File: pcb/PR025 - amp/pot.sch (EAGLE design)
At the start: 25 parts, among them IC1 LM317, IC2 LM337, X1 22-23-2031, X2 22-23-2021

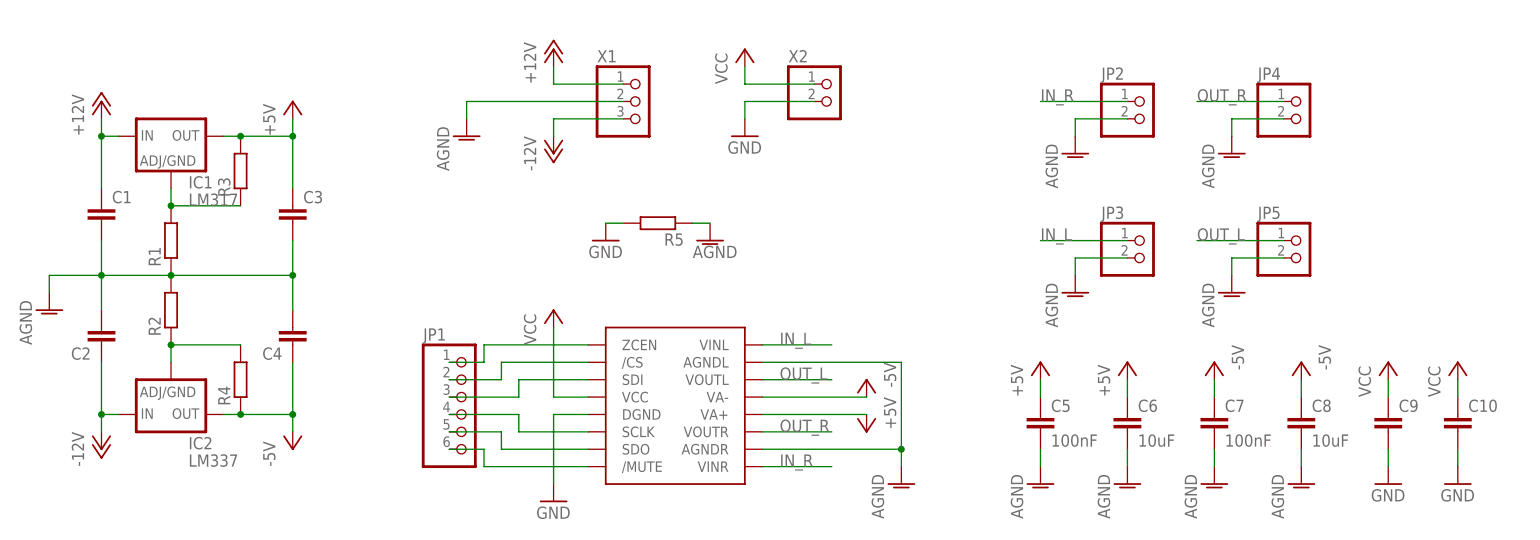
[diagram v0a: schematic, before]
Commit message: 
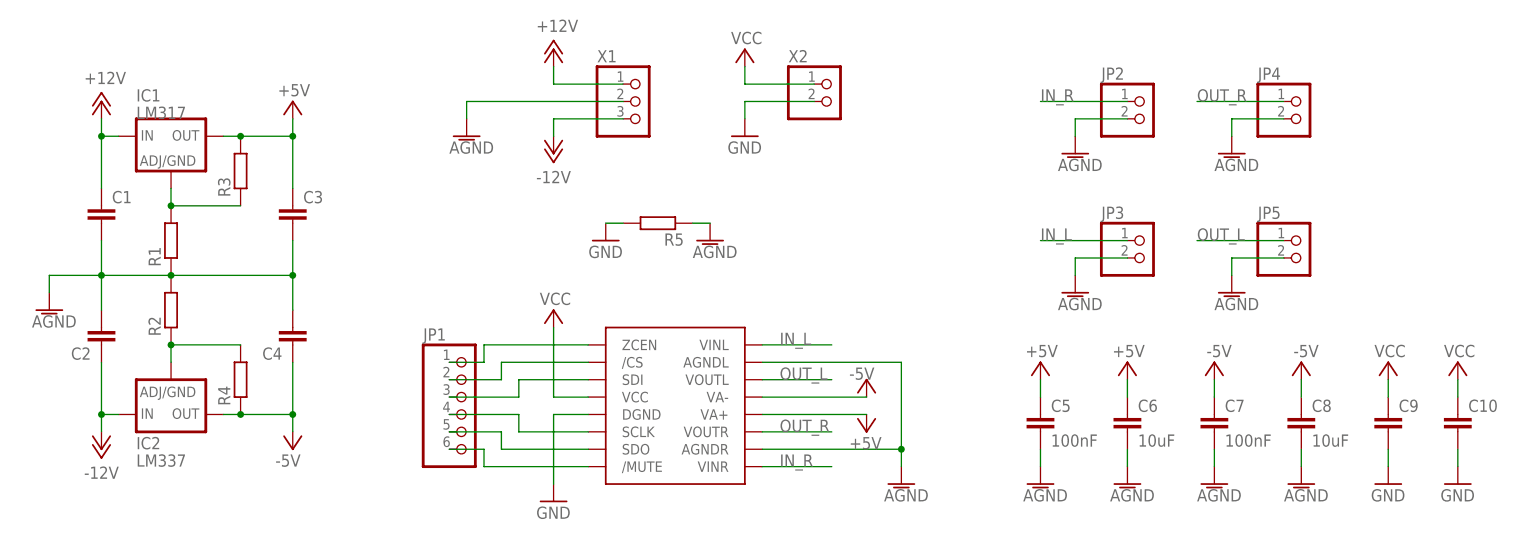
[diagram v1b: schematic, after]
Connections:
- net N$10 renamed SDO
- net N$11 renamed SCLK
- net N$6 renamed ZCEN
- net N$7 renamed /CS
- net N$8 renamed SDI
- net N$9 renamed /MUTE

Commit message: 
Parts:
- C1, C2: value (none) -> 1uF
- C10: value (none) -> 100nF
- C3, C4, C9: value (none) -> 10uF
- R1, R2: value (none) -> 680
- R3, R4: value (none) -> 220
- R5: value (none) -> 0
- U1: value (none) -> PGA2311
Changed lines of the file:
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@@
 <?xml version="1.0" encoding="utf-8"?>
 <!DOCTYPE eagle SYSTEM "eagle.dtd">
-<eagle version="6.5.0">
+<eagle version="6.6.0">
 <drawing>
 <settings>
@@
 <part name="AGND6" library="amp" deviceset="AGND" device="" value="AGND"/>
 <part name="AGND10" library="amp" deviceset="AGND" device="" value="AGND"/>
-<part name="U1" library="amp" deviceset="PGA2311" device=""/>
+<part name="U1" library="amp" deviceset="PGA2311" device="" value="PGA2311"/>
 <part name="AGND4" library="amp" deviceset="AGND" device="" value="AGND"/>
 <part name="C5" library="amp" deviceset="C-EU" device="C0805K" value="100nF"/>
@@
 <part name="IC1" library="amp" deviceset="LM317" device=""/>
 <part name="IC2" library="amp" deviceset="LM337" device=""/>
-<part name="R3" library="amp" deviceset="R-EU_" device=""/>
+<part name="R3" library="amp" deviceset="R-EU_" device="" value="220"/>
 <part name="P+7" library="amp" deviceset="+5V" device=""/>
 <part name="P+8" library="amp" deviceset="+5V" device=""/>
@@
 <part name="AGND12" library="amp" deviceset="AGND" device="" value="AGND"/>
 <part name="P+6" library="amp" deviceset="+5V" device=""/>
-<part name="R1" library="amp" deviceset="R-EU_" device=""/>
-<part name="R2" library="amp" deviceset="R-EU_" device=""/>
-<part name="R4" library="amp" deviceset="R-EU_" device=""/>
+<part name="R1" library="amp" deviceset="R-EU_" device="" value="680"/>
+<part name="R2" library="amp" deviceset="R-EU_" device="" value="680"/>
+<part name="R4" library="amp" deviceset="R-EU_" device="" value="220"/>
 <part name="P+1" library="amp" deviceset="+12V" device=""/>
 <part name="P-1" library="amp" deviceset="-12V" device=""/>
 <part name="P+2" library="amp" deviceset="+5V" device=""/>
-<part name="C1" library="amp" deviceset="C-EU" device="C0805K"/>
-<part name="C2" library="amp" deviceset="C-EU" device="C0805K"/>
-<part name="C4" library="amp" deviceset="C-EU" device="C0805K"/>
-<part name="C3" library="amp" deviceset="C-EU" device="C0805K"/>
+<part name="C1" library="amp" deviceset="C-EU" device="C0805K" value="1uF"/>
+<part name="C2" library="amp" deviceset="C-EU" device="C0805K" value="1uF"/>
+<part name="C4" library="amp" deviceset="C-EU" device="C0805K" value="10uF"/>
+<part name="C3" library="amp" deviceset="C-EU" device="C0805K" value="10uF"/>
 <part name="AGND1" library="amp" deviceset="AGND" device=""/>
 <part name="GND2" library="amp" deviceset="GND" device=""/>
-<part name="R5" library="amp" deviceset="R-EU_" device=""/>
+<part name="R5" library="amp" deviceset="R-EU_" device="" value="0"/>
 <part name="AGND3" library="amp" deviceset="AGND" device="" value="AGND"/>
 <part name="GND1" library="amp" deviceset="GND" device=""/>
 <part name="X2" library="amp" deviceset="22-23-2021" device="" value=""/>
 <part name="GND3" library="amp" deviceset="GND" device=""/>
-<part name="C9" library="amp" deviceset="C-EU" device="C0805K"/>
-<part name="C10" library="amp" deviceset="C-EU" device="C0805K"/>
+<part name="C9" library="amp" deviceset="C-EU" device="C0805K" value="10uF"/>
+<part name="C10" library="amp" deviceset="C-EU" device="C0805K" value="100nF"/>
 <part name="GND4" library="amp" deviceset="GND" device=""/>
 <part name="GND5" library="amp" deviceset="GND" device=""/>
@@
 </instance>
 <instance part="C2" gate="G$1" x="-12.7" y="134.62" smashed="yes" rot="R180">
-<attribute name="NAME" x="-14.224" y="134.239" size="1.778" layer="95" rot="R180"/>
-<attribute name="VALUE" x="-14.224" y="139.319" size="1.778" layer="96" rot="R180"/>
+<attribute name="NAME" x="-11.176" y="137.541" size="1.778" layer="95"/>
+<attribute name="VALUE" x="-11.176" y="132.461" size="1.778" layer="96"/>
 </instance>
 <instance part="C4" gate="G$1" x="15.24" y="134.62" smashed="yes" rot="R180">
-<attribute name="NAME" x="13.716" y="134.239" size="1.778" layer="95" rot="R180"/>
-<attribute name="VALUE" x="13.716" y="139.319" size="1.778" layer="96" rot="R180"/>
+<attribute name="NAME" x="16.764" y="137.541" size="1.778" layer="95"/>
+<attribute name="VALUE" x="16.764" y="132.461" size="1.778" layer="96"/>
 </instance>
 <instance part="C3" gate="G$1" x="15.24" y="154.94" smashed="yes">
